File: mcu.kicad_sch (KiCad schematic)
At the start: 41 parts, among them U1 STM32U5G9ZJTxQ, Y1 NX2016SA-16MHZ-EXS00A-CS07826, Y2 NX2012SA-32.768K-STD-MUB-1

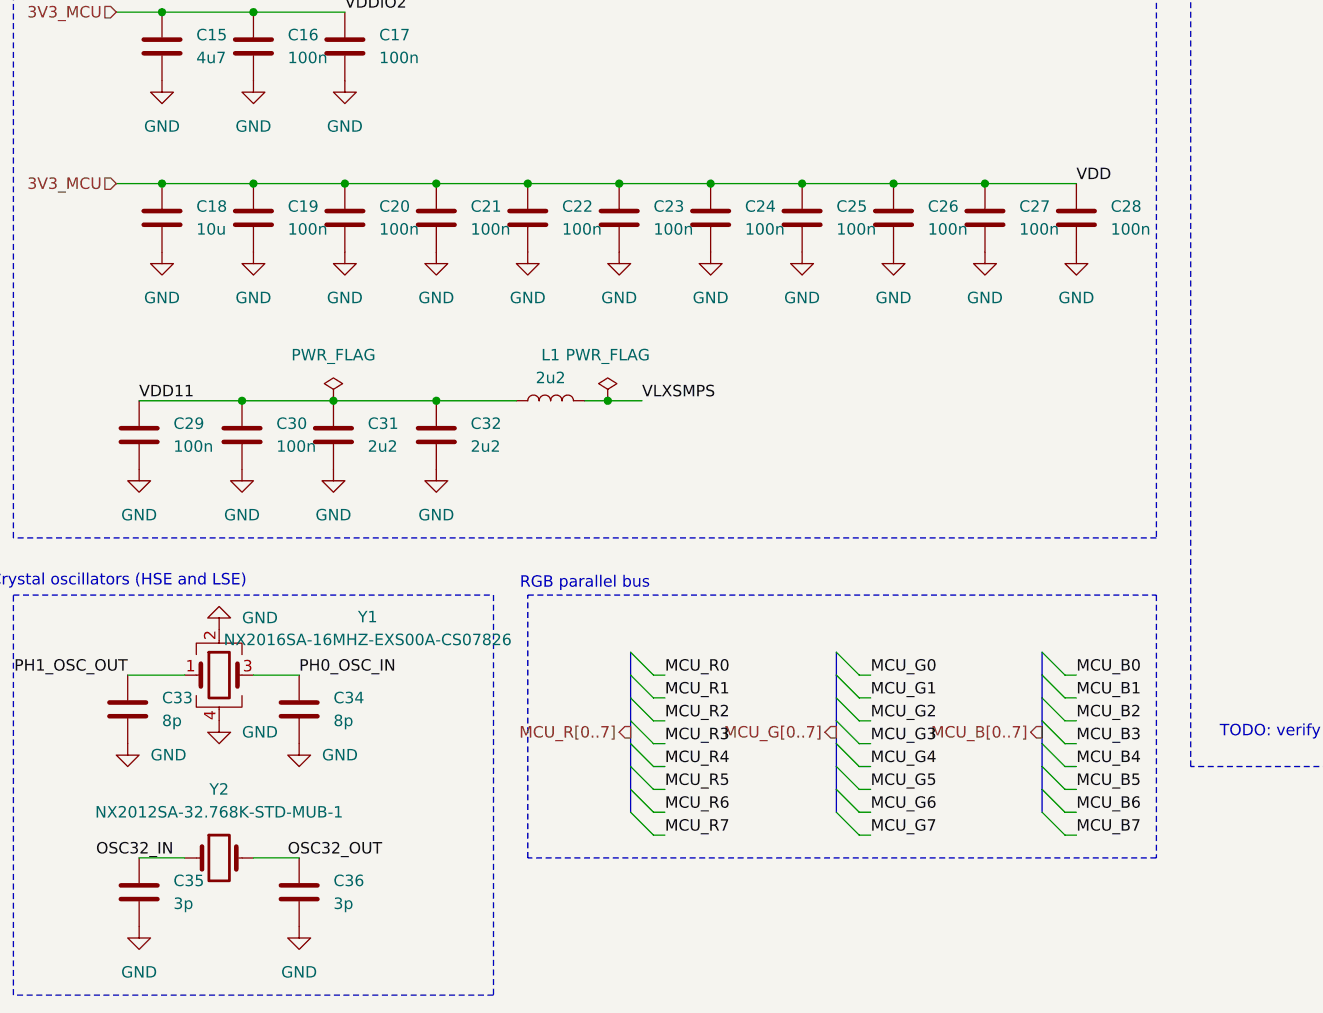
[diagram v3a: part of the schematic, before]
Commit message: Place MCU and its components around
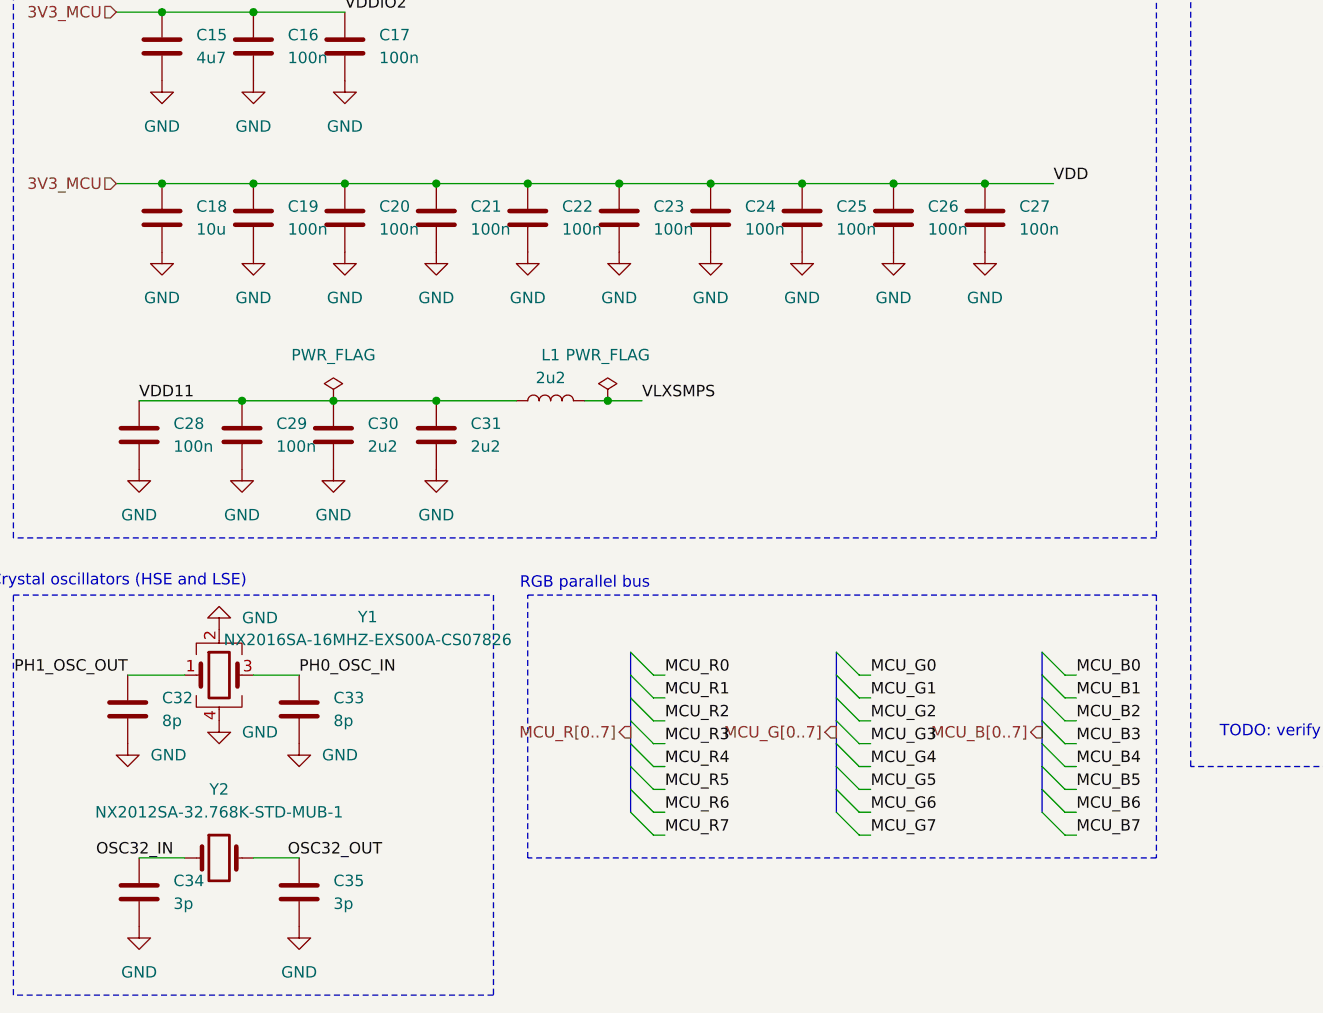
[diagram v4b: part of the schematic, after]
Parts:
- removed C28: 100n, Capacitor_SMD:C_0603_1608Metric_Pad1.08x0.95mm_HandSolder, symbol Device:C
- renumbered C29 to C28, C30 to C29, C31 to C30, C32 to C31, C33 to C32, C34 to C33, C35 to C34, C36 to C35
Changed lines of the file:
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@@
 	(wire
 		(pts
-			(xy 170.18 175.26) (xy 180.34 175.26)
+			(xy 170.18 175.26) (xy 177.8 175.26)
 		)
 		(stroke
@@
 	)
 	(label "VDD"
-		(at 180.34 175.26 0)
+		(at 177.8 175.26 0)
 		(effects
 			(font
@@
 		(dnp no)
 		(fields_autoplaced yes)
-		(property "Reference" "#PWR049"
+		(property "Reference" "#PWR048"
 			(at 87.63 213.36 0)
 			(effects
@@
 			(project "weather-station-poc"
 				(path "/38eb53bb-294e-46e4-ad59-fd355ca373b9/5f00b1ab-9f48-4782-8810-a8d68b4e6a2f"
-					(reference "#PWR049")
+					(reference "#PWR048")
 					(unit 1)
 				)
@@
 		(dnp no)
 		(fields_autoplaced yes)
-		(property "Reference" "C36"
+		(property "Reference" "C35"
 			(at 97.79 252.7299 0)
 			(effects
@@
 			(project "weather-station-poc"
 				(path "/38eb53bb-294e-46e4-ad59-fd355ca373b9/5f00b1ab-9f48-4782-8810-a8d68b4e6a2f"
-					(reference "C36")
+					(reference "C35")
 					(unit 1)
 				)
@@
 		(dnp no)
 		(fields_autoplaced yes)
-		(property "Reference" "#PWR057"
+		(property "Reference" "#PWR056"
 			(at 76.2 264.16 0)
 			(effects
@@
 			(project "weather-station-poc"
 				(path "/38eb53bb-294e-46e4-ad59-fd355ca373b9/5f00b1ab-9f48-4782-8810-a8d68b4e6a2f"
-					(reference "#PWR057")
+					(reference "#PWR056")
 					(unit 1)
 				)
@@
 		(dnp no)
 		(fields_autoplaced yes)
-		(property "Reference" "#PWR054"
+		(property "Reference" "#PWR053"
 			(at 85.09 241.3 0)
 			(effects
@@
 			(project "weather-station-poc"
 				(path "/38eb53bb-294e-46e4-ad59-fd355ca373b9/5f00b1ab-9f48-4782-8810-a8d68b4e6a2f"
-					(reference "#PWR054")
+					(reference "#PWR053")
 					(unit 1)
 				)
@@
 		(dnp no)
 		(fields_autoplaced yes)
-		(property "Reference" "#PWR048"
+		(property "Reference" "#PWR047"
 			(at 76.2 213.36 0)
 			(effects
@@
 			(project "weather-station-poc"
 				(path "/38eb53bb-294e-46e4-ad59-fd355ca373b9/5f00b1ab-9f48-4782-8810-a8d68b4e6a2f"
-					(reference "#PWR048")
+					(reference "#PWR047")
 					(unit 1)
 				)
@@
 		(dnp no)
 		(fields_autoplaced yes)
-		(property "Reference" "#PWR051"
+		(property "Reference" "#PWR050"
 			(at 109.22 213.36 0)
 			(effects
@@
 			(project "weather-station-poc"
 				(path "/38eb53bb-294e-46e4-ad59-fd355ca373b9/5f00b1ab-9f48-4782-8810-a8d68b4e6a2f"
-					(reference "#PWR051")
+					(reference "#PWR050")
 					(unit 1)
 				)
@@
 		(dnp no)
 		(fields_autoplaced yes)
-		(property "Reference" "#PWR052"
+		(property "Reference" "#PWR051"
 			(at 85.09 218.44 0)
 			(effects
@@
 			(project "weather-station-poc"
 				(path "/38eb53bb-294e-46e4-ad59-fd355ca373b9/5f00b1ab-9f48-4782-8810-a8d68b4e6a2f"
-					(reference "#PWR052")
+					(reference "#PWR051")
 					(unit 1)
 				)
@@
 		(dnp no)
 		(fields_autoplaced yes)
-		(property "Reference" "C32"
+		(property "Reference" "C31"
 			(at 113.03 201.9299 0)
 			(effects
@@
 			(project "weather-station-poc"
 				(path "/38eb53bb-294e-46e4-ad59-fd355ca373b9/5f00b1ab-9f48-4782-8810-a8d68b4e6a2f"
-					(reference "C32")
+					(reference "C31")
 					(unit 1)
 				)
@@
 	(symbol
 		(lib_id "Device:C")
-		(at 180.34 179.07 0)
-		(unit 1)
-		(exclude_from_sim no)
-		(in_bom yes)
-		(on_board yes)
-		(dnp no)
-		(fields_autoplaced yes)
-		(property "Reference" "C28"
-			(at 184.15 177.7999 0)
-			(effects
-				(font
-					(size 1.27 1.27)
-				)
-				(justify left)
-			)
-		)
-		(property "Value" "100n"
-			(at 184.15 180.3399 0)
-			(effects
-				(font
-					(size 1.27 1.27)
-				)
-				(justify left)
-			)
-		)
-		(property "Footprint" "Capacitor_SMD:C_0603_1608Metric_Pad1.08x0.95mm_HandSolder"
-			(at 181.3052 182.88 0)
-			(effects
-				(font
-					(size 1.27 1.27)
-				)
-				(hide yes)
-			)
-		)
-		(property "Datasheet" "~"
-			(at 180.34 179.07 0)
-			(effects
-				(font
-					(size 1.27 1.27)
-				)
-				(hide yes)
-			)
-		)
-		(property "Description" "Unpolarized capacitor"
-			(at 180.34 179.07 0)
-			(effects
-				(font
-					(size 1.27 1.27)
-				)
-				(hide yes)
-			)
-		)
-		(pin "2"
-		)
-		(pin "1"
-		)
-		(instances
-			(project "weather-station-poc"
-				(path "/38eb53bb-294e-46e4-ad59-fd355ca373b9/5f00b1ab-9f48-4782-8810-a8d68b4e6a2f"
-					(reference "C28")
-					(unit 1)
-				)
-			)
-		)
-	)
-	(symbol
-		(lib_id "Device:C")
 		(at 74.93 233.68 180)
 		(unit 1)
@@
 		(dnp no)
 		(fields_autoplaced yes)
-		(property "Reference" "C33"
+		(property "Reference" "C32"
 			(at 78.74 232.4099 0)
 			(effects
@@
 			(project ""
 				(path "/38eb53bb-294e-46e4-ad59-fd355ca373b9/5f00b1ab-9f48-4782-8810-a8d68b4e6a2f"
-					(reference "C33")
+					(reference "C32")
 					(unit 1)
 				)
@@
 		(dnp no)
 		(fields_autoplaced yes)
-		(property "Reference" "#PWR056"
+		(property "Reference" "#PWR055"
 			(at 93.98 243.84 0)
 			(effects
@@
 			(project "weather-station-poc"
 				(path "/38eb53bb-294e-46e4-ad59-fd355ca373b9/5f00b1ab-9f48-4782-8810-a8d68b4e6a2f"
-					(reference "#PWR056")
+					(reference "#PWR055")
 					(unit 1)
 				)
@@
 		(dnp no)
 		(fields_autoplaced yes)
-		(property "Reference" "#PWR053"
+		(property "Reference" "#PWR052"
 			(at 280.67 238.76 0)
 			(effects
@@
 			(project ""
 				(path "/38eb53bb-294e-46e4-ad59-fd355ca373b9/5f00b1ab-9f48-4782-8810-a8d68b4e6a2f"
-					(reference "#PWR053")
+					(reference "#PWR052")
 					(unit 1)
 				)
@@
 		(dnp no)
 		(fields_autoplaced yes)
-		(property "Reference" "#PWR050"
+		(property "Reference" "#PWR049"
 			(at 97.79 213.36 0)
 			(effects
@@
 			(project "weather-station-poc"
 				(path "/38eb53bb-294e-46e4-ad59-fd355ca373b9/5f00b1ab-9f48-4782-8810-a8d68b4e6a2f"
-					(reference "#PWR050")
+					(reference "#PWR049")
 					(unit 1)
 				)
@@
 		(dnp no)
 		(fields_autoplaced yes)
-		(property "Reference" "#PWR058"
+		(property "Reference" "#PWR057"
 			(at 93.98 264.16 0)
 			(effects
@@
 			(project "weather-station-poc"
 				(path "/38eb53bb-294e-46e4-ad59-fd355ca373b9/5f00b1ab-9f48-4782-8810-a8d68b4e6a2f"
-					(reference "#PWR058")
+					(reference "#PWR057")
 					(unit 1)
 				)
@@
 		(dnp no)
 		(fields_autoplaced yes)
-		(property "Reference" "C34"
+		(property "Reference" "C33"
 			(at 97.79 232.4099 0)
 			(effects
@@
 			(project "weather-station-poc"
 				(path "/38eb53bb-294e-46e4-ad59-fd355ca373b9/5f00b1ab-9f48-4782-8810-a8d68b4e6a2f"
-					(reference "C34")
+					(reference "C33")
 					(unit 1)
 				)
@@
 	)
 	(symbol
-		(lib_id "power:GND")
-		(at 180.34 182.88 0)
-		(unit 1)
-		(exclude_from_sim no)
-		(in_bom yes)
-		(on_board yes)
-		(dnp no)
-		(fields_autoplaced yes)
-		(property "Reference" "#PWR047"
-			(at 180.34 189.23 0)
-			(effects
-				(font
-					(size 1.27 1.27)
-				)
-				(hide yes)
-			)
-		)
-		(property "Value" "GND"
-			(at 180.34 187.96 0)
-			(effects
-				(font
-					(size 1.27 1.27)
-				)
-			)
-		)
-		(property "Footprint" ""
-			(at 180.34 182.88 0)
-			(effects
-				(font
-					(size 1.27 1.27)
-				)
-				(hide yes)
-			)
-		)
-		(property "Datasheet" ""
-			(at 180.34 182.88 0)
-			(effects
-				(font
-					(size 1.27 1.27)
-				)
-				(hide yes)
-			)
-		)
-		(property "Description" "Power symbol creates a global label with name \"GND\" , ground"
-			(at 180.34 182.88 0)
-			(effects
-				(font
-					(size 1.27 1.27)
-				)
-				(hide yes)
-			)
-		)
-		(pin "1"
-		)
-		(instances
-			(project "weather-station-poc"
-				(path "/38eb53bb-294e-46e4-ad59-fd355ca373b9/5f00b1ab-9f48-4782-8810-a8d68b4e6a2f"
-					(reference "#PWR047")
-					(unit 1)
-				)
-			)
-		)
-	)
-	(symbol
 		(lib_id "Device:C")
 		(at 78.74 143.51 0)
@@
 		(dnp no)
 		(fields_autoplaced yes)
-		(property "Reference" "#PWR055"
+		(property "Reference" "#PWR054"
 			(at 74.93 243.84 0)
 			(effects
@@
 			(project "weather-station-poc"
 				(path "/38eb53bb-294e-46e4-ad59-fd355ca373b9/5f00b1ab-9f48-4782-8810-a8d68b4e6a2f"
-					(reference "#PWR055")
+					(reference "#PWR054")
 					(unit 1)
 				)
@@
 		(dnp no)
 		(fields_autoplaced yes)
-		(property "Reference" "C30"
+		(property "Reference" "C29"
 			(at 91.44 201.9299 0)
 			(effects
@@
 			(project "weather-station-poc"
 				(path "/38eb53bb-294e-46e4-ad59-fd355ca373b9/5f00b1ab-9f48-4782-8810-a8d68b4e6a2f"
-					(reference "C30")
+					(reference "C29")
 					(unit 1)
 				)
@@
 		(dnp no)
 		(fields_autoplaced yes)
-		(property "Reference" "C29"
+		(property "Reference" "C28"
 			(at 80.01 201.9299 0)
 			(effects
@@
 			(project "weather-station-poc"
 				(path "/38eb53bb-294e-46e4-ad59-fd355ca373b9/5f00b1ab-9f48-4782-8810-a8d68b4e6a2f"
-					(reference "C29")
+					(reference "C28")
 					(unit 1)
 				)
@@
 		(dnp no)
 		(fields_autoplaced yes)
-		(property "Reference" "C31"
+		(property "Reference" "C30"
 			(at 101.6 201.9299 0)
 			(effects
@@
 			(project "weather-station-poc"
 				(path "/38eb53bb-294e-46e4-ad59-fd355ca373b9/5f00b1ab-9f48-4782-8810-a8d68b4e6a2f"
-					(reference "C31")
+					(reference "C30")
 					(unit 1)
 				)
@@
 		(dnp no)
 		(fields_autoplaced yes)
-		(property "Reference" "C35"
+		(property "Reference" "C34"
 			(at 80.01 252.7299 0)
 			(effects
@@
 			(project "weather-station-poc"
 				(path "/38eb53bb-294e-46e4-ad59-fd355ca373b9/5f00b1ab-9f48-4782-8810-a8d68b4e6a2f"
-					(reference "C35")
+					(reference "C34")
 					(unit 1)
 				)
